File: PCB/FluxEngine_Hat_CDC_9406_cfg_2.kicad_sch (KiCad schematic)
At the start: 6 parts, among them J1 CY8CKIT-059, P1 FDD_IBMPC_host, P2 FDD_SA800_host

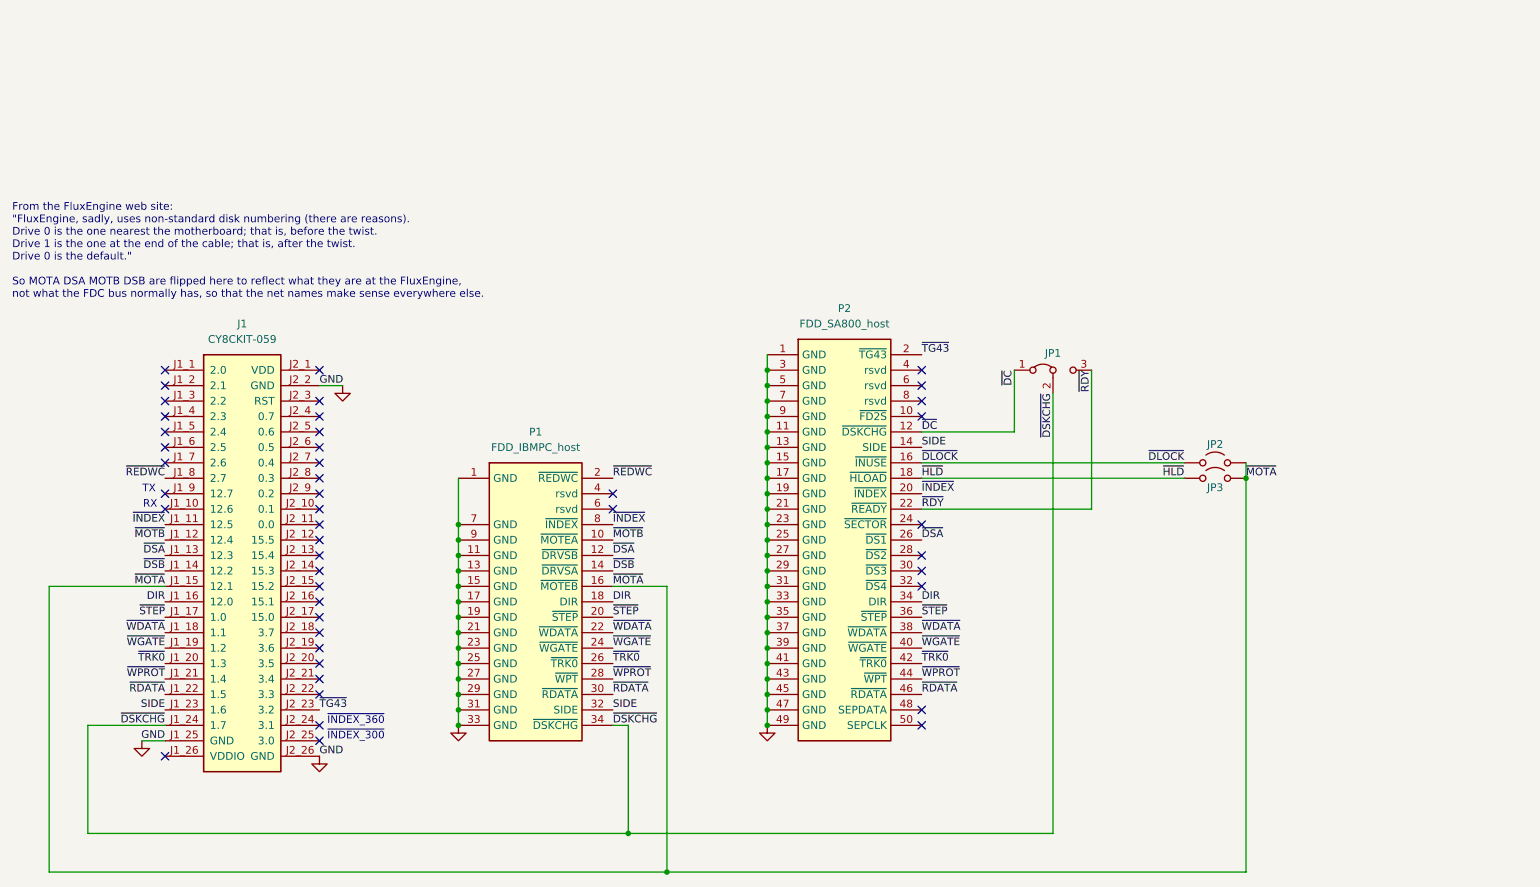
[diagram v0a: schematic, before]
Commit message: add CDC9406 type 1 & 2
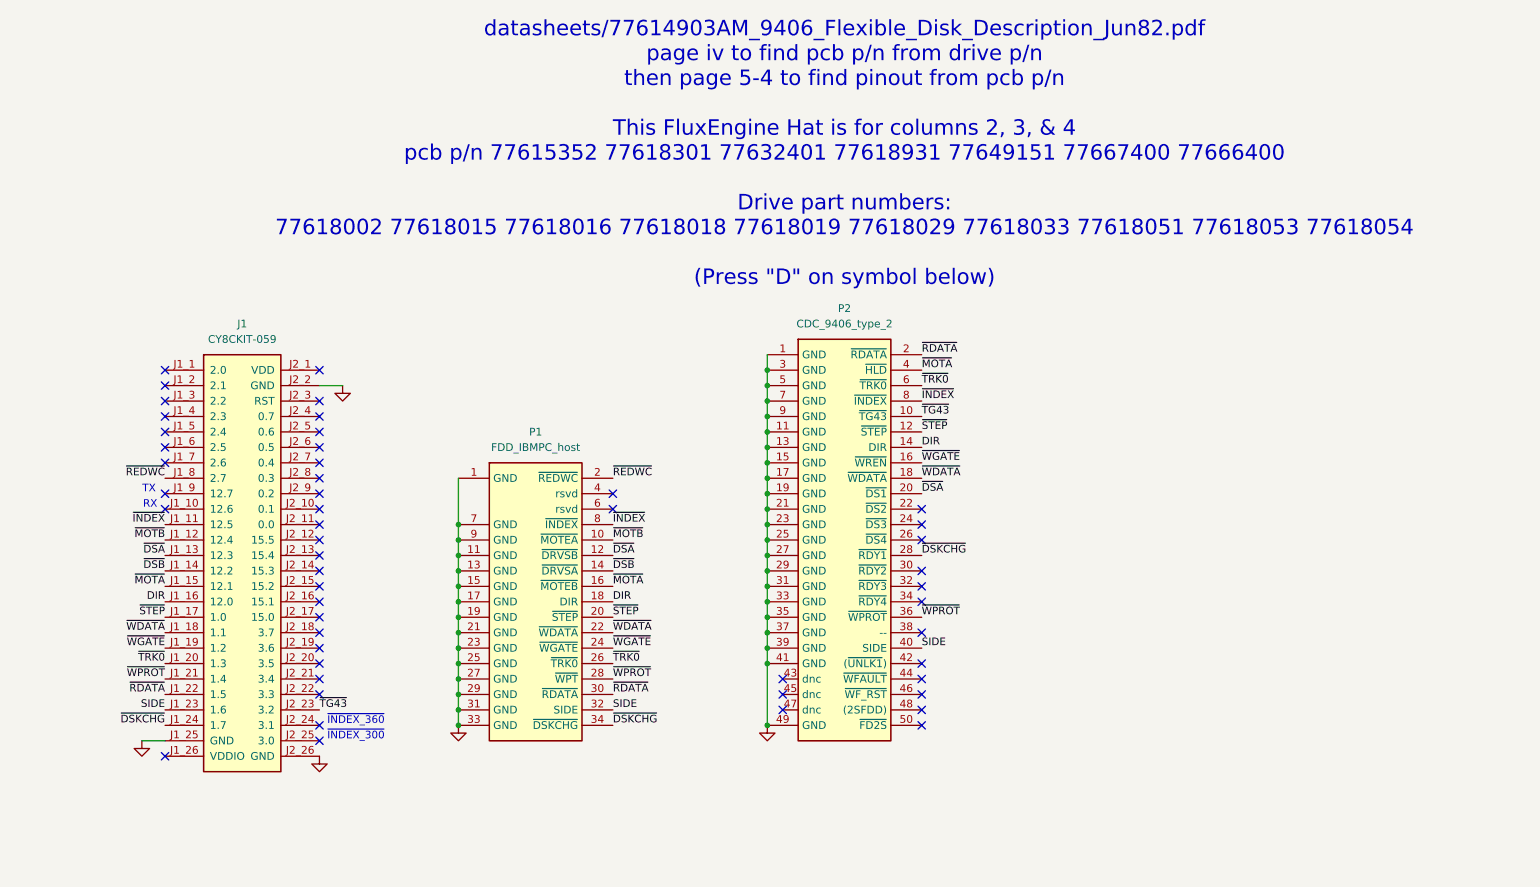
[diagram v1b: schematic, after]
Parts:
- removed JP1: Jumper_3_Bridged12, 000_LOCAL:PinHeader_1x03_P2.54mm_Vertical, symbol 000_LOCAL:Jumper_3_Bridged12
- removed JP2, JP3: Jumper_2_Open, 000_LOCAL:PinHeader_1x02_P2.54mm_Vertical, symbol 000_LOCAL:Jumper_2_Open
- P2: value FDD_SA800_host -> CDC_9406_type_2; symbol 000_LOCAL:FDD_SA800_host -> 000_LOCAL:FDD_CDC_9406_pinout_2
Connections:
- net ~{DC} is gone; now on net ~{STEP}: P2.12 (~{STEP})
- net ~{DLOCK} is gone; now on net ~{WGATE}: P2.16 (~{WREN})
- net ~{HLD} is gone; now on net ~{WDATA}: P2.18 (~{WDATA})
- net DIR: now also P2.14 (DIR); no longer P2.34 (DIR)
- net GND: no longer P2.43 (GND), P2.45 (GND), P2.47 (GND)
- net SIDE: now also P2.40 (SIDE); no longer P2.14 (SIDE)
- net ~{DSA}: now also P2.20 (~{DS1}); no longer P2.26 (~{DS1})
- net ~{DSKCHG}: now also P2.28 (~{RDY1})
- net ~{INDEX}: now also P2.8 (~{INDEX}); no longer P2.20 (~{INDEX})
- net ~{MOTA}: now also P2.4 (~{HLD})
- net ~{RDATA}: now also P2.2 (~{RDATA}); no longer P2.46 (~{RDATA})
- net ~{STEP}: no longer P2.36 (~{STEP})
- net ~{TG43}: now also P2.10 (~{TG43}); no longer P2.2 (~{TG43})
- net ~{TRK0}: now also P2.6 (~{TRK0}); no longer P2.42 (~{TRK0})
- net ~{WDATA}: no longer P2.38 (~{WDATA})
- net ~{WGATE}: no longer P2.40 (~{WGATE})
- net ~{WPROT}: now also P2.36 (~{WPROT}); no longer P2.44 (~{WPT})
- net ~{RDY}: no longer names the net of P2.22 (~{DS2})
- no-connect marks 45 -> 50
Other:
- note added: "datasheets/77614903AM_9406_Flexible_Disk_Description_Jun82.pdf page iv to find pcb p/n from drive p/n then page 5-4 to find pinout from pcb p/n This FluxEngine Hat is for columns 2, 3, & 4 pcb p/n 77615352 77618301 77632401 77618931 77649151 77667400 77666400 Drive part numbers: 77618002 77618015 77618016 77618018 77618019 77618029 77618033 77618051 77618053 77618054 (Press "D" on symbol below)"
- note removed: "From the FluxEngine web site: "FluxEngine, sadly, uses non-standard disk numbering (there are reasons). Drive 0 is the one nearest the motherboard; that is, before the twist. Drive 1 is the one at the end of the cable; that is, after the twist. Drive 0 is the default." So MOTA DSA MOTB DSB are flipped here to reflect what they are at the FluxEngine, not what the FDC bus normally has, so that the 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"
- title: FluxEngine_Hat for PC and SA800 -> FluxEngine_Hat for PC and CDC-9406 cfg 2
